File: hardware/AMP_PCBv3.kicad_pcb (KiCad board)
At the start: 2 copper layers, 70 x 56.5 mm, 2 parts, among them CN10 Male_R2, CN7 Male_L1

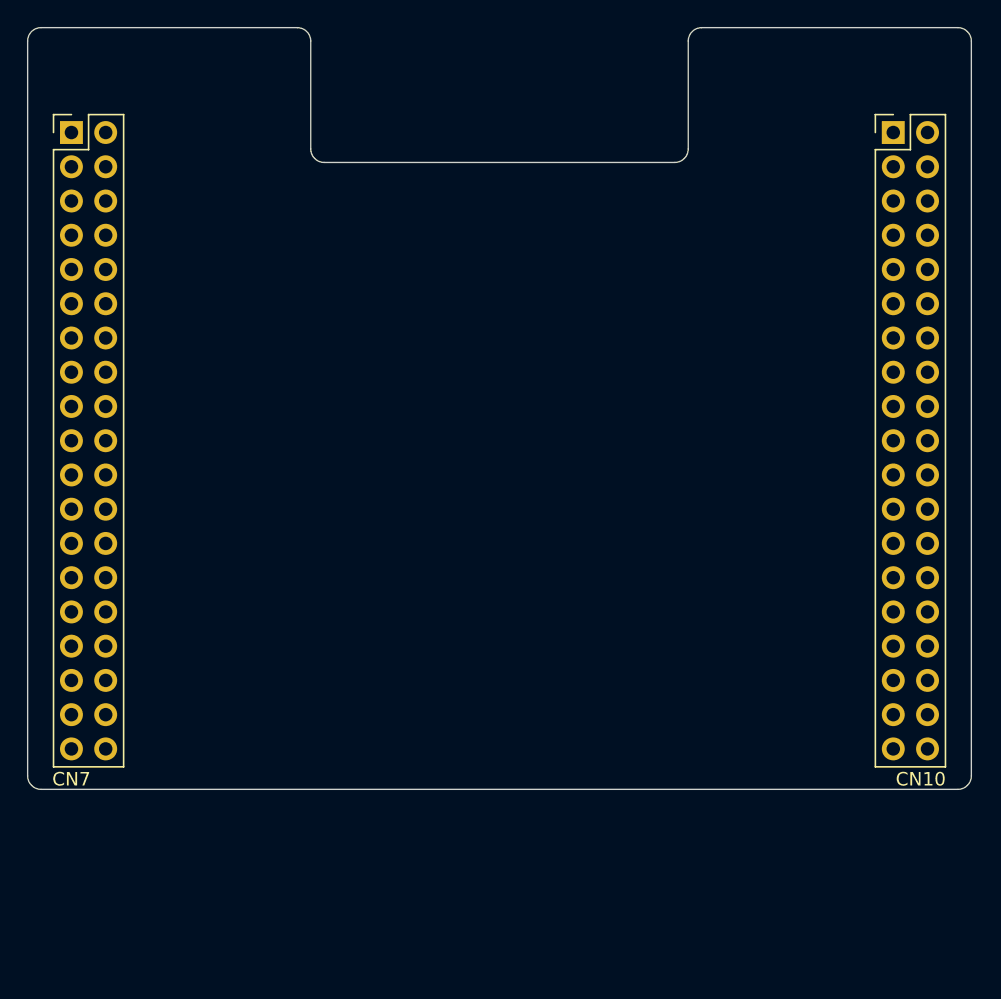
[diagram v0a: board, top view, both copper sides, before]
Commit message: Add power circuitry and begin routing
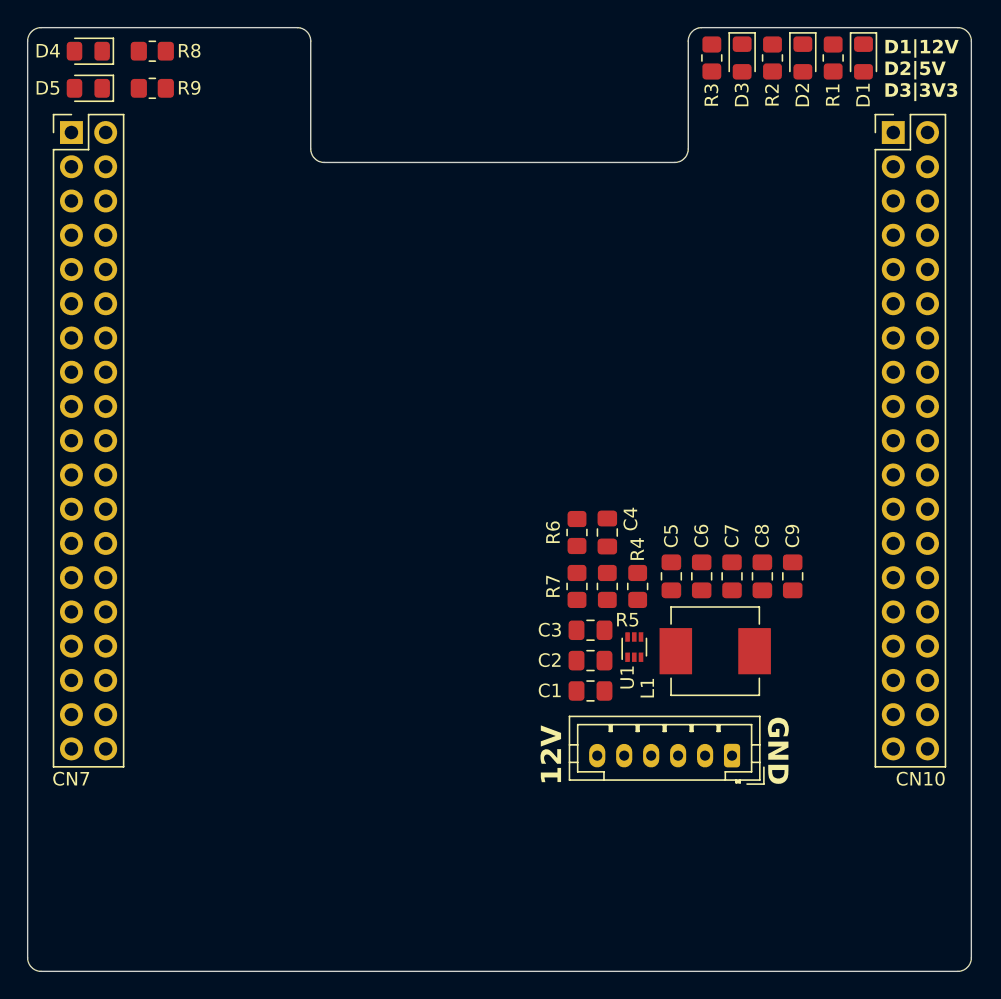
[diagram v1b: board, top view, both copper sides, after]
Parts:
- added C1: 10uF, Capacitor_SMD:C_0805_2012Metric_Pad1.18x1.45mm_HandSolder, F.Cu at (150.5, 117.7)
- added C2: 10uF, Capacitor_SMD:C_0805_2012Metric_Pad1.18x1.45mm_HandSolder, F.Cu at (150.5, 115.5)
- added C3: 100nF, Capacitor_SMD:C_0805_2012Metric_Pad1.18x1.45mm_HandSolder, F.Cu at (150.5, 113.2)
- added C4: 33pF, Capacitor_SMD:C_0805_2012Metric_Pad1.18x1.45mm_HandSolder, F.Cu at (151.8, 106.0)
- added C5: 22uF, Capacitor_SMD:C_0805_2012Metric_Pad1.18x1.45mm_HandSolder, F.Cu at (156.5, 109.2)
- added C6: 22uF, Capacitor_SMD:C_0805_2012Metric_Pad1.18x1.45mm_HandSolder, F.Cu at (158.8, 109.2)
- added C7: 22uF, Capacitor_SMD:C_0805_2012Metric_Pad1.18x1.45mm_HandSolder, F.Cu at (161.0, 109.2)
- added C8: 22uF, Capacitor_SMD:C_0805_2012Metric_Pad1.18x1.45mm_HandSolder, F.Cu at (163.2, 109.2)
- added C9: 100nF, Capacitor_SMD:C_0805_2012Metric_Pad1.18x1.45mm_HandSolder, F.Cu at (165.5, 109.2)
- added D1: PWR_12V, LED_SMD:LED_0805_2012Metric_Pad1.15x1.40mm_HandSolder, F.Cu at (170.8, 70.8)
- added D2: PWR_5V, LED_SMD:LED_0805_2012Metric_Pad1.15x1.40mm_HandSolder, F.Cu at (166.2, 70.8)
- added D3: PWR_3V3, LED_SMD:LED_0805_2012Metric_Pad1.15x1.40mm_HandSolder, F.Cu at (161.8, 70.8)
- added D4: STAT1, LED_SMD:LED_0805_2012Metric_Pad1.15x1.40mm_HandSolder, F.Cu at (113.2, 70.2)
- added D5: STAT2, LED_SMD:LED_0805_2012Metric_Pad1.15x1.40mm_HandSolder, F.Cu at (113.2, 73.0)
- added J1: Input_PWR, Connector_JST:JST_PH_B6B-PH-K_1x06_P2.00mm_Vertical, F.Cu at (161.0, 122.5)
- added L1: 2.2uH, Inductor_SMD:L_Vishay_IHLP-2525, F.Cu at (159.8, 114.8)
- added R1: 2k, Resistor_SMD:R_0805_2012Metric_Pad1.20x1.40mm_HandSolder, F.Cu at (168.5, 70.8)
- added R2: 600, Resistor_SMD:R_0805_2012Metric_Pad1.20x1.40mm_HandSolder, F.Cu at (164.0, 70.8)
- added R3: 260, Resistor_SMD:R_0805_2012Metric_Pad1.20x1.40mm_HandSolder, F.Cu at (159.5, 70.8)
- added R4: 100k, Resistor_SMD:R_0805_2012Metric_Pad1.20x1.40mm_HandSolder, F.Cu at (154.0, 110.0)
- added R5: 15.8k, Resistor_SMD:R_0805_2012Metric_Pad1.20x1.40mm_HandSolder, F.Cu at (151.8, 110.0)
- added R6: 220k, Resistor_SMD:R_0805_2012Metric_Pad1.20x1.40mm_HandSolder, F.Cu at (149.5, 106.0)
- added R7: 30k, Resistor_SMD:R_0805_2012Metric_Pad1.20x1.40mm_HandSolder, F.Cu at (149.5, 110.0)
- added R8: 260, Resistor_SMD:R_0805_2012Metric_Pad1.20x1.40mm_HandSolder, F.Cu at (118.0, 70.2)
- added R9: 260, Resistor_SMD:R_0805_2012Metric_Pad1.20x1.40mm_HandSolder, F.Cu at (118.0, 73.0)
- added U1: TPS56624x, Package_TO_SOT_SMD:SOT-563, F.Cu at (153.8, 114.5)
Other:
- board size 70 x 56.5 mm -> 70 x 70 mm
- board text added: "12V"
- board text added: "D1|12V D2|5V D3|3V3"
- board text added: "GND"

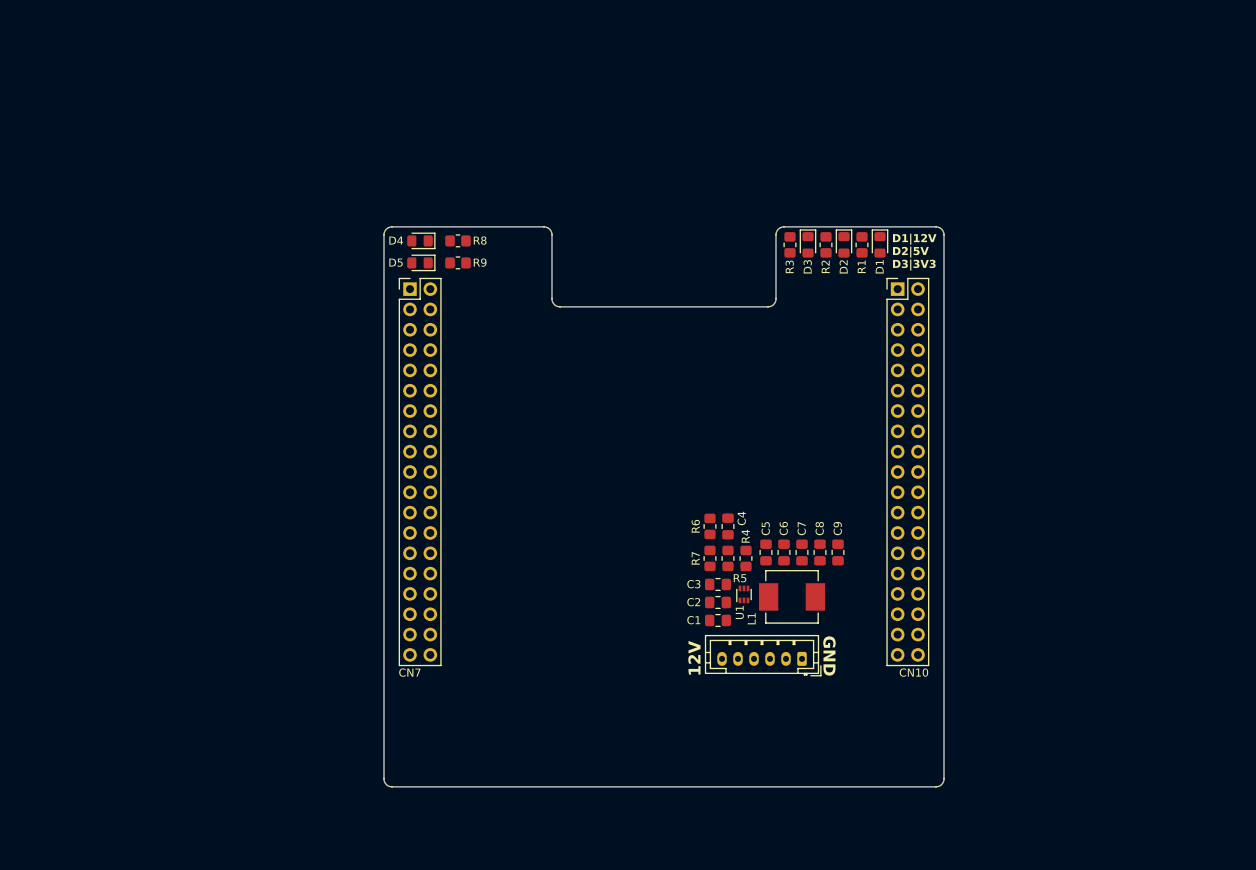
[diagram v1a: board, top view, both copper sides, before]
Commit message: Add USB/UART and more routing
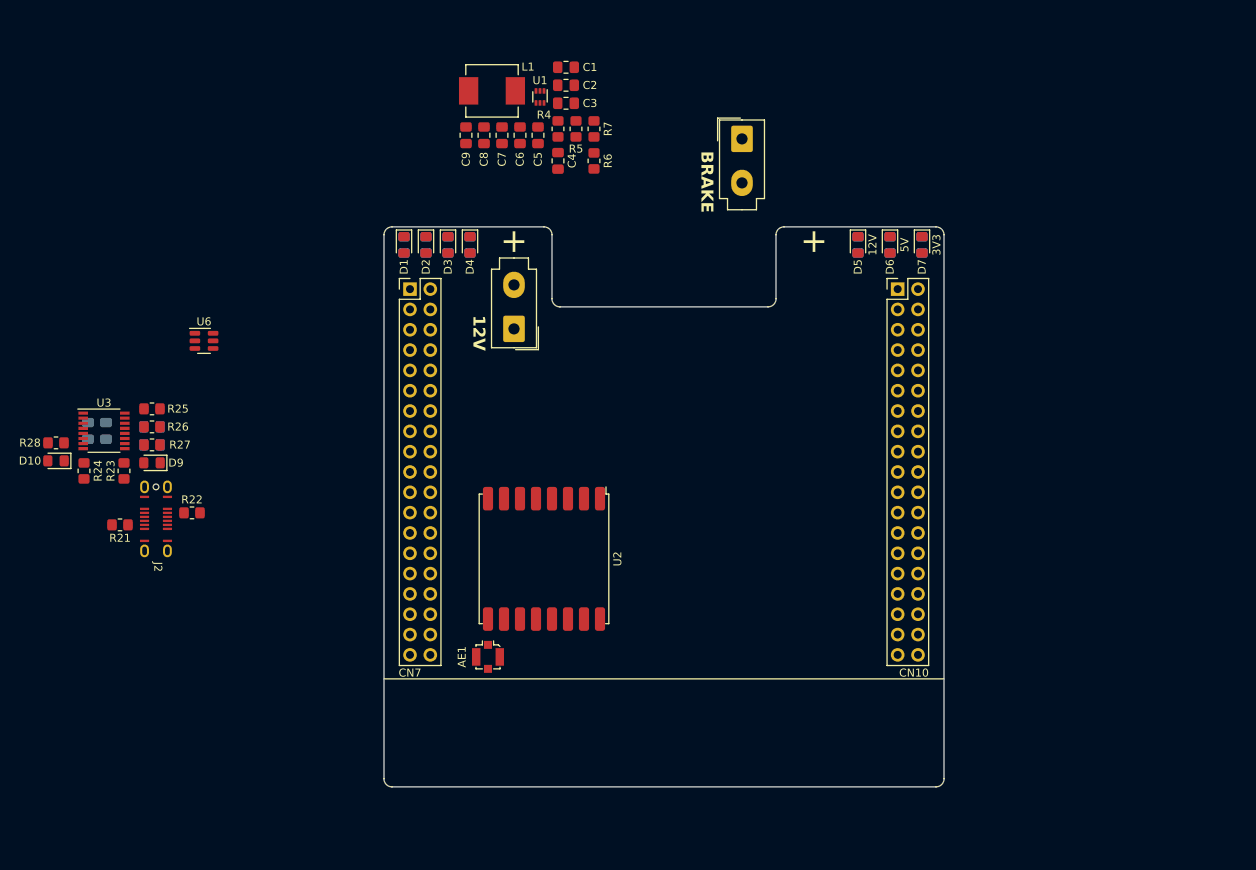
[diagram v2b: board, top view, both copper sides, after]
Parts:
- added AE1: 915MHz, Connector_Coaxial:U.FL_Molex_MCRF_73412-0110_Vertical, F.Cu at (121.8, 122.2)
- added C21: 100nF, Capacitor_SMD:C_0805_2012Metric_Pad1.18x1.45mm_HandSolder, B.Cu at (74.0, 94.0)
- added C22: 4.7uF, Capacitor_SMD:C_0805_2012Metric_Pad1.18x1.45mm_HandSolder, B.Cu at (79.8, 95.8)
- added C23: 100nF, Capacitor_SMD:C_0805_2012Metric_Pad1.18x1.45mm_HandSolder, B.Cu at (71.8, 94.0)
- added C24: 100nF, Capacitor_SMD:C_0805_2012Metric_Pad1.18x1.45mm_HandSolder, B.Cu at (79.8, 93.5)
- added D10: TX, LED_SMD:LED_0805_2012Metric_Pad1.15x1.40mm_HandSolder, F.Cu at (67.8, 97.8)
- added D3: STAT3, LED_SMD:LED_0805_2012Metric_Pad1.15x1.40mm_HandSolder, F.Cu at (116.8, 70.8)
- added D4: STAT4, LED_SMD:LED_0805_2012Metric_Pad1.15x1.40mm_HandSolder, F.Cu at (119.5, 70.8)
- added D9: RX, LED_SMD:LED_0805_2012Metric_Pad1.15x1.40mm_HandSolder, F.Cu at (79.8, 98.0)
- added J2: USB_C_Receptacle_USB2.0_16P, AMP_Custom:USB_C_Receptacle_GCT_USB4145, F.Cu at (81.7, 105.0)
- added M1: 12V, Connector_Molex:Molex_Mini-Fit_Jr_5566-02A_2x01_P4.20mm_Vertical, F.Cu at (153.5, 57.5)
- added R10: 260, Resistor_SMD:R_0805_2012Metric_Pad1.20x1.40mm_HandSolder, B.Cu at (116.8, 70.8)
- added R11: 260, Resistor_SMD:R_0805_2012Metric_Pad1.20x1.40mm_HandSolder, B.Cu at (119.5, 70.8)
- added R21: 5.1k, Resistor_SMD:R_0805_2012Metric_Pad1.20x1.40mm_HandSolder, F.Cu at (75.8, 105.8)
- added R22: 5.1k, Resistor_SMD:R_0805_2012Metric_Pad1.20x1.40mm_HandSolder, F.Cu at (84.8, 104.2)
- added R23: 27, Resistor_SMD:R_0805_2012Metric_Pad1.20x1.40mm_HandSolder, F.Cu at (76.2, 99.0)
- added R24: 27, Resistor_SMD:R_0805_2012Metric_Pad1.20x1.40mm_HandSolder, F.Cu at (71.2, 99.0)
- added R25: 4k7, Resistor_SMD:R_0805_2012Metric_Pad1.20x1.40mm_HandSolder, F.Cu at (79.8, 91.2)
- added R26: 10k, Resistor_SMD:R_0805_2012Metric_Pad1.20x1.40mm_HandSolder, F.Cu at (79.8, 93.5)
- added R27: 270, Resistor_SMD:R_0805_2012Metric_Pad1.20x1.40mm_HandSolder, F.Cu at (79.8, 95.8)
- added R28: 270, Resistor_SMD:R_0805_2012Metric_Pad1.20x1.40mm_HandSolder, F.Cu at (67.8, 95.5)
- added U2: RFM95W-915S2, RF_Module:HOPERF_RFM9XW_SMD, F.Cu at (128.8, 110.0)
- added U3: FT230XS, Package_SO:SSOP-16_3.9x4.9mm_P0.635mm, F.Cu at (73.8, 94.0)
- added U6: USBLC6-2SC6, Package_TO_SOT_SMD:SOT-23-6, F.Cu at (86.2, 82.8)
- J1: footprint Connector_JST:JST_PH_B6B-PH-K_1x06_P2.00mm_Vertical -> Connector_Molex:Molex_Mini-Fit_Jr_5566-02A_2x01_P4.20mm_Vertical
- R1, R2, R3, R8, R9: moved to B.Cu
- moved L1 73.5 mm to (122.2, 51.5), turned to 180 degrees
- moved C1 71.7 mm to (131.5, 48.5), turned to 0 degrees
- moved C9 69.9 mm to (119.0, 57.0), turned to -90 degrees
- moved C2 67.4 mm to (131.5, 50.8), turned to 0 degrees
- moved U1 67.2 mm to (128.2, 52.2), turned to -90 degrees
- moved C8 67.0 mm to (121.2, 57.0), turned to -90 degrees
- moved C7 64.2 mm to (123.5, 57.0), turned to -90 degrees
- moved C3 63.1 mm to (131.5, 53.0), turned to 0 degrees
- moved C6 61.7 mm to (125.8, 57.0), turned to -90 degrees
- moved C5 59.4 mm to (128.0, 57.0), turned to -90 degrees
- moved R4 58.6 mm to (130.5, 56.2), turned to -90 degrees
- moved R5 57.0 mm to (132.8, 56.2), turned to -90 degrees
- moved R7 55.6 mm to (135.0, 56.2), turned to 90 degrees
- moved J1 54.7 mm to (125.0, 81.2)
- moved C4 50.4 mm to (130.5, 60.2), turned to 90 degrees
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- renumbered D4 to D1, D5 to D2, D1 to D5, D2 to D6, D3 to D7
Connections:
- C4 pad 1: +5V -> /E5V
- C5 pad 1: +5V -> /E5V
- C6 pad 1: +5V -> /E5V
- C7 pad 1: +5V -> /E5V
- C8 pad 1: +5V -> /E5V
- C9 pad 1: +5V -> /E5V
- J1 pad 2: GND -> +12V
- L1 pad 2: +5V -> /E5V
- R6 pad 1: +5V -> /E5V
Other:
- board text added: "+"
- board text added: "3V3"
- board text added: "5V"
- board text added: "BRAKE"
- board text removed: "D1|12V D2|5V D3|3V3"
- board text removed: "GND"

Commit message: Add new brake controller and inductor 3D model
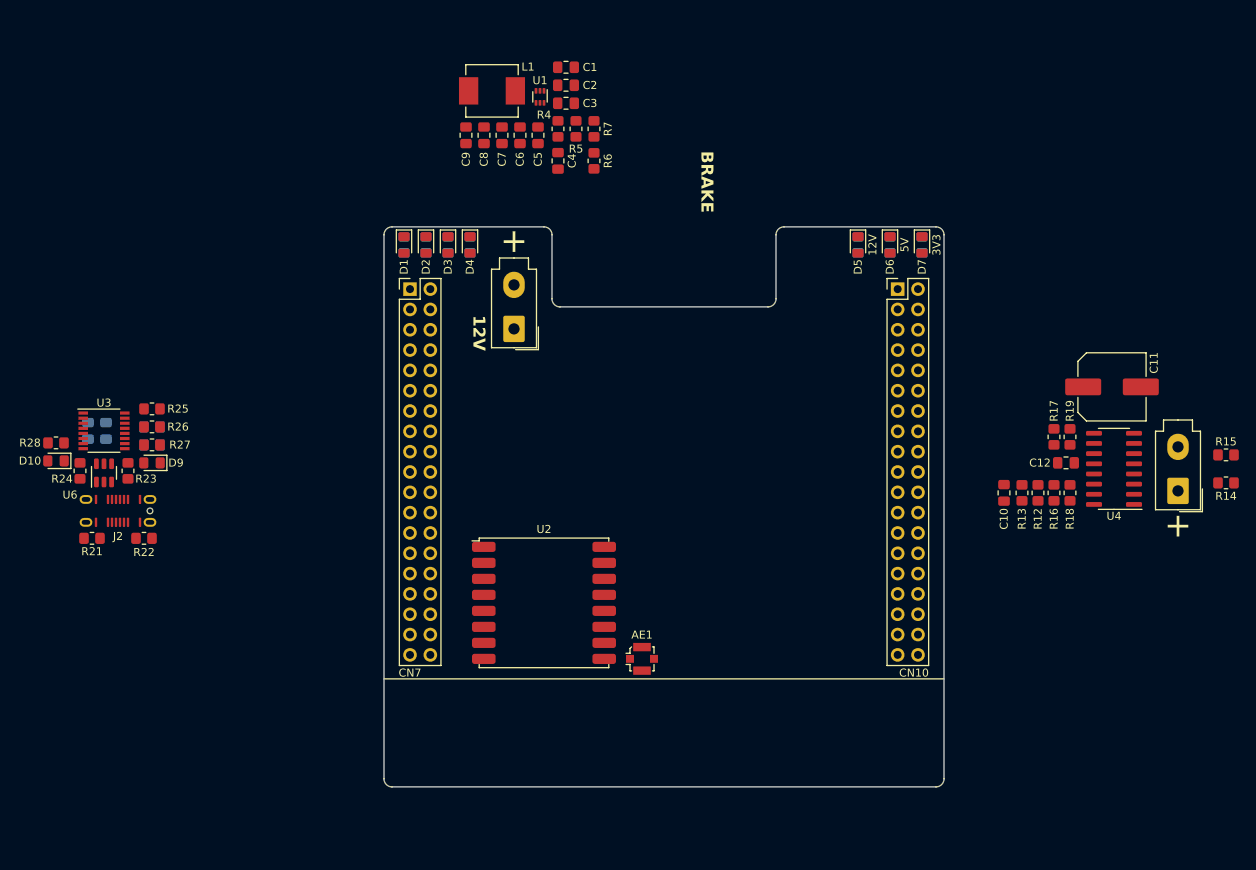
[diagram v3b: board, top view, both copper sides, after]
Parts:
- added C10: 33nF, Capacitor_SMD:C_0805_2012Metric_Pad1.18x1.45mm_HandSolder, F.Cu at (186.2, 101.8)
- added C11: 250uF, Capacitor_SMD:C_Elec_8x10.2, F.Cu at (199.8, 88.5)
- added C12: 100nF, Capacitor_SMD:C_0805_2012Metric_Pad1.18x1.45mm_HandSolder, F.Cu at (194.0, 98.0)
- added R12: 1.5k, Resistor_SMD:R_0805_2012Metric_Pad1.20x1.40mm_HandSolder, F.Cu at (190.5, 101.8)
- added R13: 10k, Resistor_SMD:R_0805_2012Metric_Pad1.20x1.40mm_HandSolder, F.Cu at (188.5, 101.8)
- added R14: 1k, Resistor_SMD:R_0805_2012Metric_Pad1.20x1.40mm_HandSolder, F.Cu at (214.0, 100.5)
- added R15: 1k, Resistor_SMD:R_0805_2012Metric_Pad1.20x1.40mm_HandSolder, F.Cu at (214.0, 97.0)
- added R16: 1k, Resistor_SMD:R_0805_2012Metric_Pad1.20x1.40mm_HandSolder, F.Cu at (192.5, 101.8)
- added R17: 1k, Resistor_SMD:R_0805_2012Metric_Pad1.20x1.40mm_HandSolder, F.Cu at (192.5, 94.8)
- added R18: 3.3k, Resistor_SMD:R_0805_2012Metric_Pad1.20x1.40mm_HandSolder, F.Cu at (194.5, 101.8)
- added R19: 3.3k, Resistor_SMD:R_0805_2012Metric_Pad1.20x1.40mm_HandSolder, F.Cu at (194.5, 94.8)
- added U4: VNH5200A-E, Package_SO:SOP-16_3.9x9.9mm_P1.27mm, F.Cu at (200.0, 98.8)
- M1: value 12V -> Brake
- moved M1 70.0 mm to (208.0, 101.5), turned to 180 degrees
- moved U6 20.7 mm to (73.8, 99.2), turned to 90 degrees
- moved AE1 19.3 mm to (141.0, 122.5), turned to -90 degrees
- moved R22 6.79 mm to (78.8, 107.4)
- moved J2 6.19 mm to (75.5, 105.4), turned to 180 degrees
- moved U2 5.50 mm to (128.8, 115.5), turned to 0 degrees
- moved R21 3.88 mm to (72.2, 107.4)
- moved R23 0.50 mm to (76.8, 99.0)
- moved R24 0.50 mm to (70.8, 99.0)
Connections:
- M1 pad 1: /Brake Controller/MOTOR+ -> Net-(M1-+)
- M1 pad 2: /Brake Controller/MOTOR- -> Net-(M1--)

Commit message: Add IMU schematic
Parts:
- added C13: 1uF, Capacitor_SMD:C_0805_2012Metric_Pad1.18x1.45mm_HandSolder, F.Cu at (86.5, 63.3)
- added C14: 100nF, Capacitor_SMD:C_0805_2012Metric_Pad1.18x1.45mm_HandSolder, F.Cu at (86.5, 66.3)
- added C15: 100nF, Capacitor_SMD:C_0805_2012Metric_Pad1.18x1.45mm_HandSolder, F.Cu at (86.5, 69.3)
- added C16: 100nF, Capacitor_SMD:C_0805_2012Metric_Pad1.18x1.45mm_HandSolder, F.Cu at (86.5, 72.3)
- added U5: ICM-20948, Sensor_Motion:InvenSense_QFN-24_3x3mm_P0.4mm, F.Cu at (91.5, 69.0)
- added U7: TLV74318P, Package_TO_SOT_SMD:SOT-23-5_HandSoldering, F.Cu at (91.8, 64.1)
